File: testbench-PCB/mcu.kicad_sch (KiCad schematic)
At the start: 16 parts, among them J2 AVR-ISP-6, SW1 RESET, U1 ATmega2561-16A, Y1 X322516MLB4SI

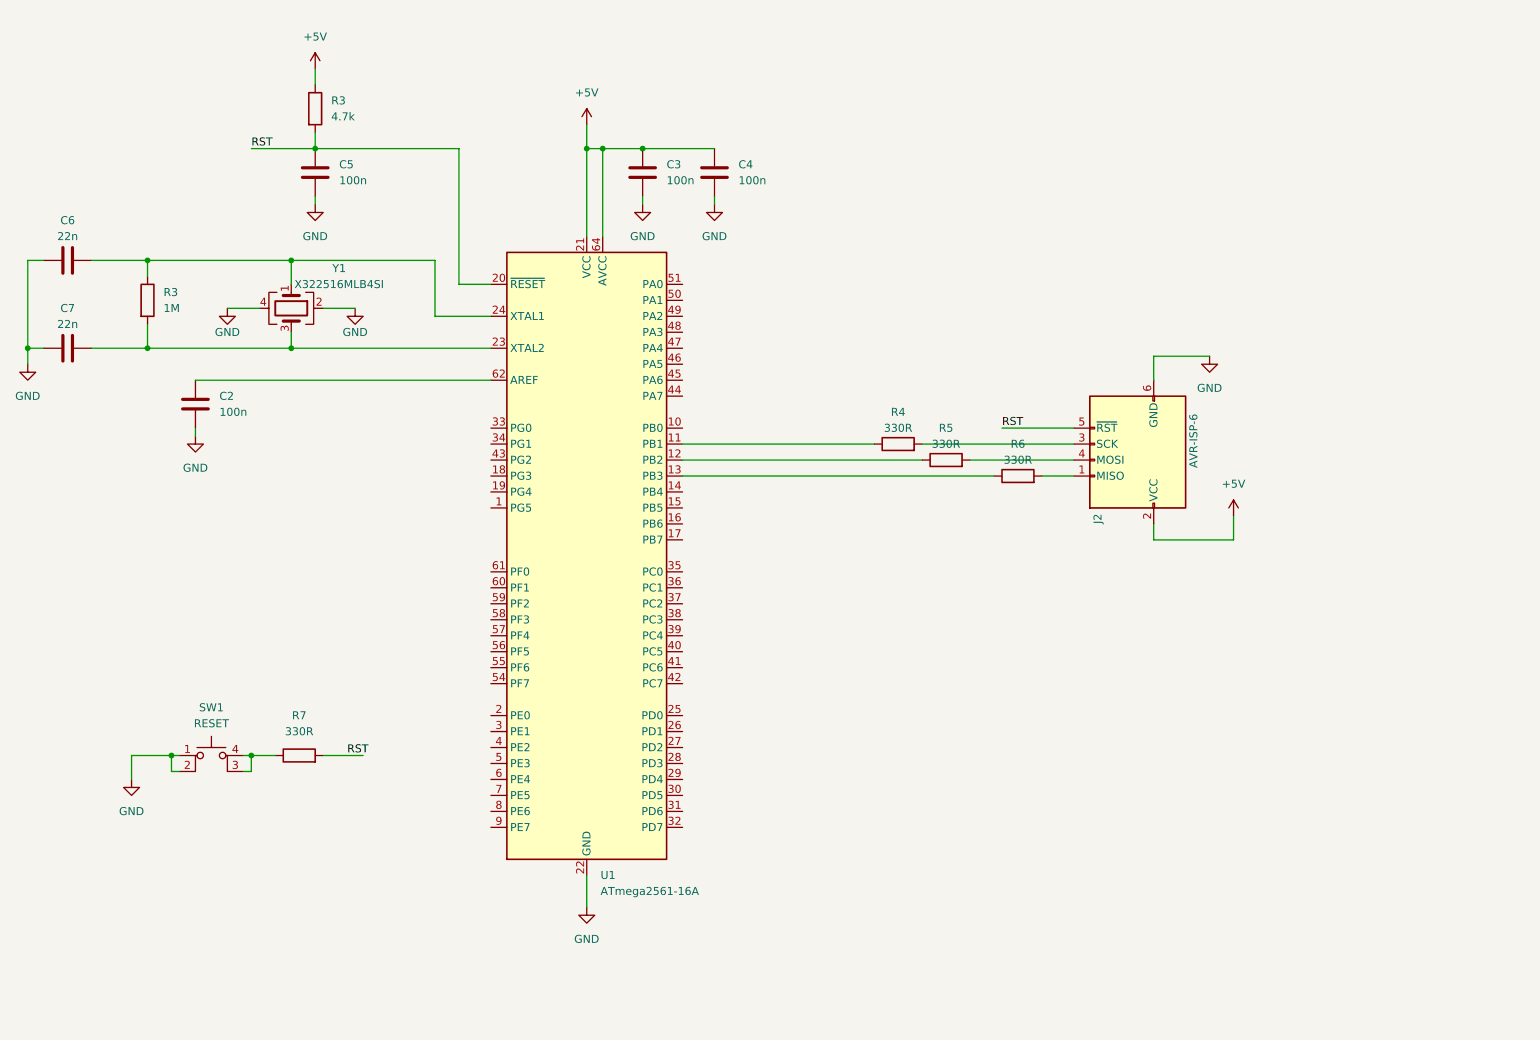
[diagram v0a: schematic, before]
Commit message: Added USB interface.
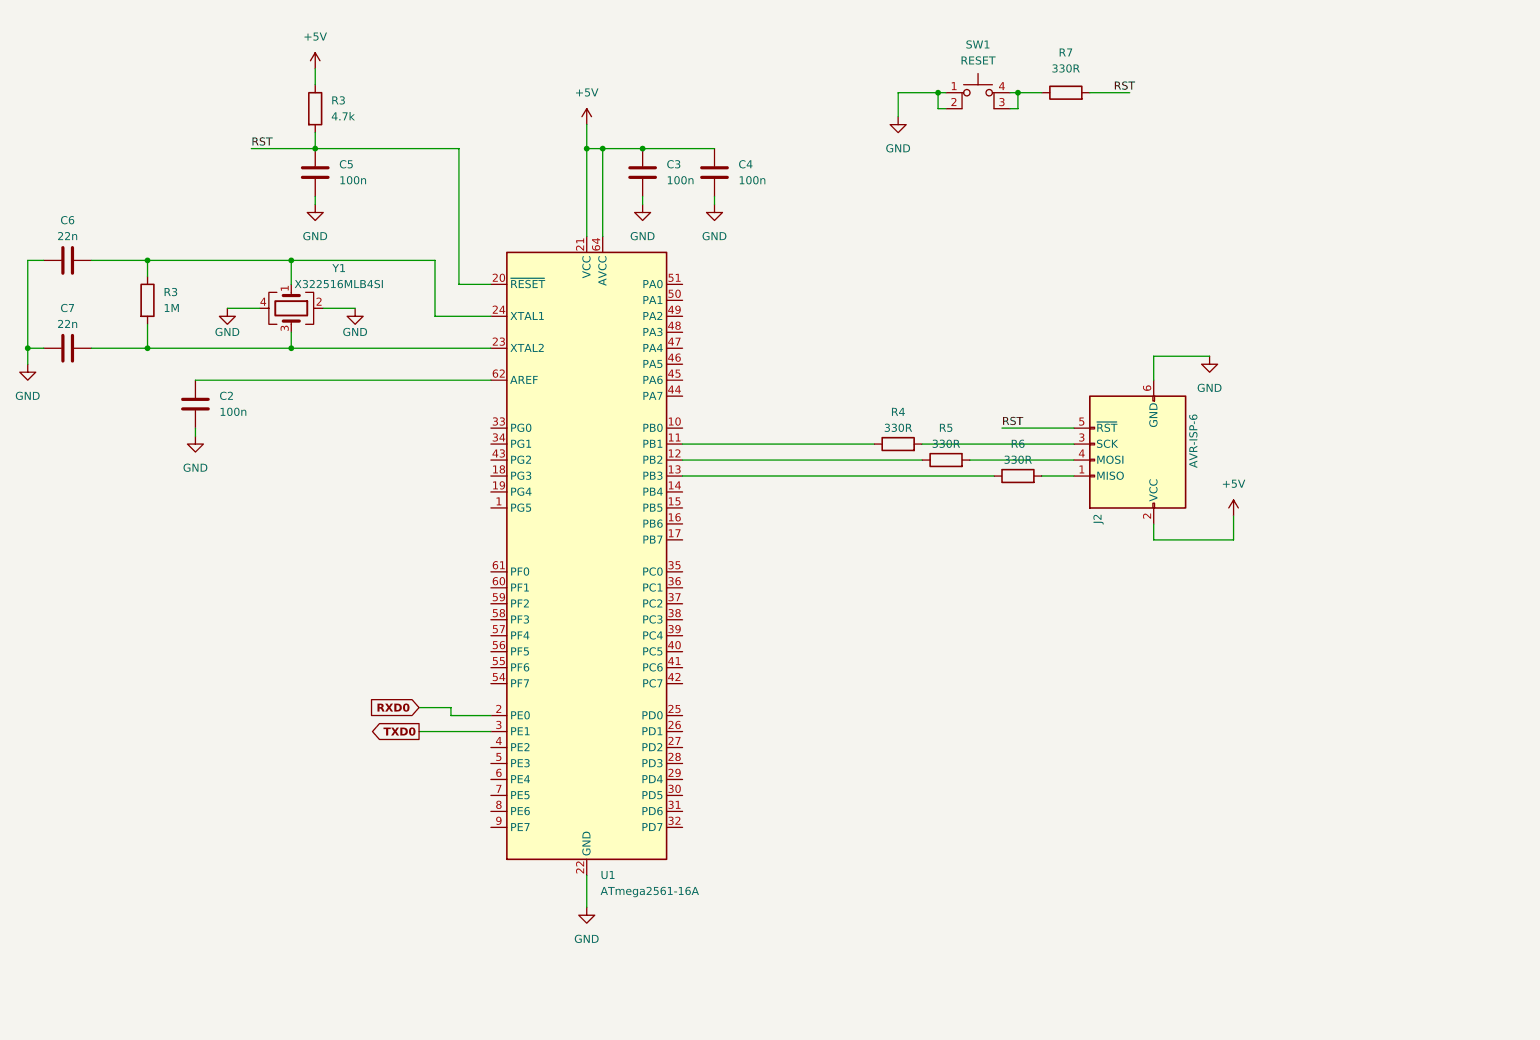
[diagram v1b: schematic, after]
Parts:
- R3, R4, R5, R6, R7: footprint (none) -> Resistor_SMD:R_0805_2012Metric
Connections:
- net RXD0: now reaches U1.2 (PE0)
- net TXD0: now reaches U1.3 (PE1)
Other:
- moved on the sheet: R7, SW1

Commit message: Added connection between some modules.
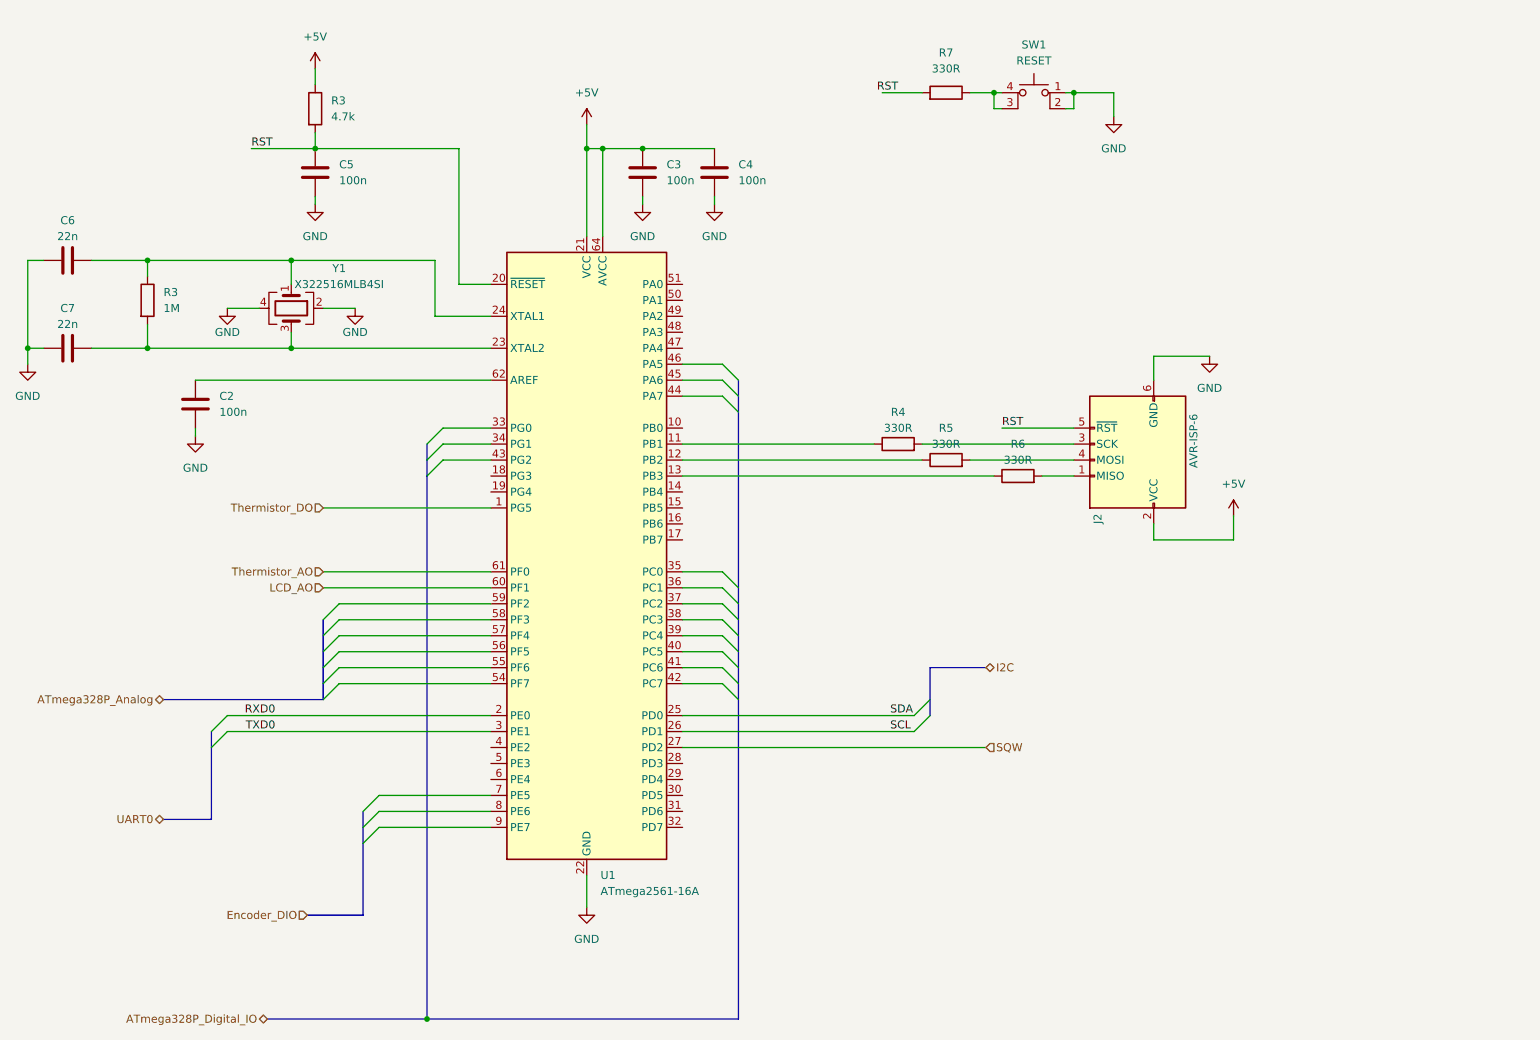
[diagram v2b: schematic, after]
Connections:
- net Thermistor_DO: now reaches U1.1 (PG5)
- net SDA: now reaches U1.25 (PD0)
- net SCL: now reaches U1.26 (PD1)
- net SQW: now reaches U1.27 (PD2)
- net LCD_AO: now reaches U1.60 (PF1)
- net Thermistor_AO: now reaches U1.61 (PF0)
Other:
- moved on the sheet: R7, SW1

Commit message: Finished connection between modules and MCU.
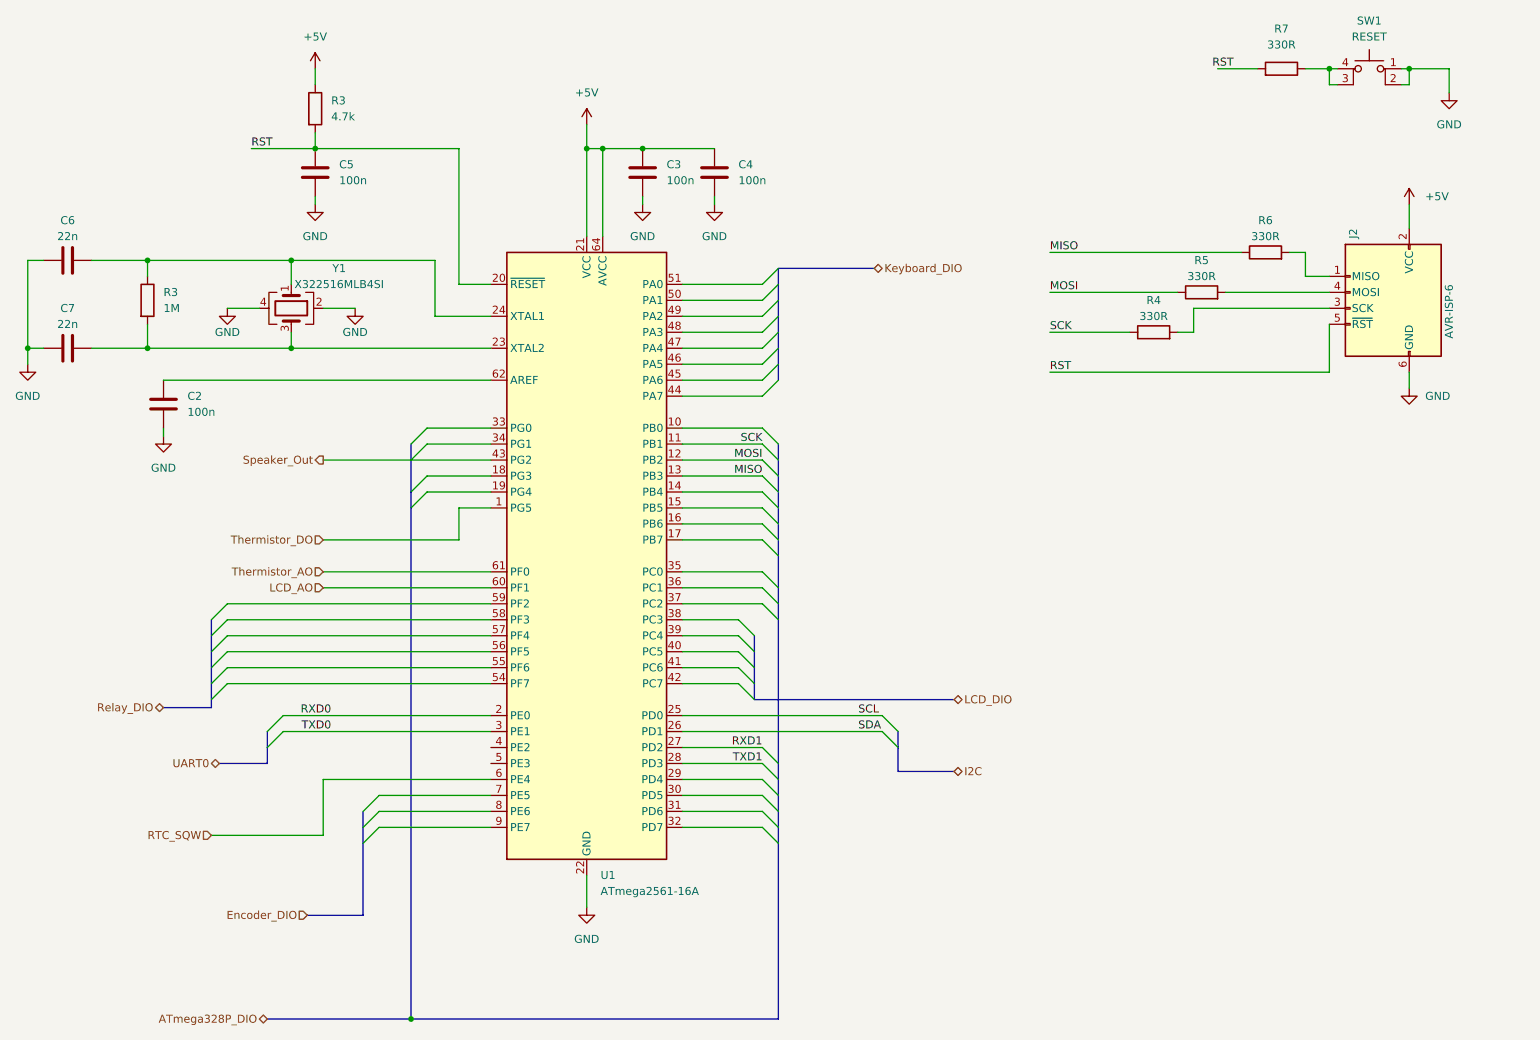
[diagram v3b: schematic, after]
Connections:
- net SCL: now also U1.25 (PD0); no longer U1.26 (PD1)
- net SDA: now also U1.26 (PD1); no longer U1.25 (PD0)
- net MOSI: now reaches R5.1, U1.12 (PB2)
- net SCK: now reaches R4.1, U1.11 (PB1)
- net MISO: now reaches R6.1, U1.13 (PB3)
- net TXD1: now reaches U1.28 (PD3)
- net Speaker_Out: now reaches U1.43 (PG2)
- net RTC_SQW: now reaches U1.6 (PE4)
- net SQW renamed RXD1
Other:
- moved on the sheet: C2, J2, R4, R5, R6, R7, SW1

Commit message: Added footprints to few parts.
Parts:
- C2, C3, C4, C5, C6, C7: footprint (none) -> Capacitor_SMD:C_0805_2012Metric
- J2: footprint (none) -> Connector_PinHeader_2.54mm:PinHeader_2x03_P2.54mm_Vertical
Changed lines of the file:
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@@
       (effects (font (size 1.27 1.27)) (justify left))
     )
-    (property "Footprint" "" (at 149.5552 53.34 0)
+    (property "Footprint" "Capacitor_SMD:C_0805_2012Metric" (at 149.5552 53.34 0)
       (effects (font (size 1.27 1.27)) hide)
     )
@@
       (effects (font (size 1.27 1.27)))
     )
-    (property "Footprint" "" (at 49.53 76.5048 0)
+    (property "Footprint" "Capacitor_SMD:C_0805_2012Metric" (at 49.53 76.5048 0)
       (effects (font (size 1.27 1.27)) hide)
     )
@@
       (effects (font (size 1.27 1.27)) (justify left))
     )
-    (property "Footprint" "" (at 138.1252 53.34 0)
+    (property "Footprint" "Capacitor_SMD:C_0805_2012Metric" (at 138.1252 53.34 0)
       (effects (font (size 1.27 1.27)) hide)
     )
@@
       (effects (font (size 1.27 1.27)))
     )
-    (property "Footprint" "" (at 49.53 62.5348 0)
+    (property "Footprint" "Capacitor_SMD:C_0805_2012Metric" (at 49.53 62.5348 0)
       (effects (font (size 1.27 1.27)) hide)
     )
@@
       (effects (font (size 1.27 1.27)) (justify left))
     )
-    (property "Footprint" "" (at 86.0552 53.34 0)
+    (property "Footprint" "Capacitor_SMD:C_0805_2012Metric" (at 86.0552 53.34 0)
       (effects (font (size 1.27 1.27)) hide)
     )
@@
       (effects (font (size 1.27 1.27)) (justify left))
     )
-    (property "Footprint" "" (at 61.9252 90.17 0)
+    (property "Footprint" "Capacitor_SMD:C_0805_2012Metric" (at 61.9252 90.17 0)
       (effects (font (size 1.27 1.27)) hide)
     )
@@
       (effects (font (size 1.27 1.27)) (justify right))
     )
-    (property "Footprint" "" (at 262.89 69.85 90)
-      (effects (font (size 1.27 1.27)) hide)
-    )
+    (property "Footprint" "Connector_PinHeader_2.54mm:PinHeader_2x03_P2.54mm_Vertical" (at 262.89 69.85 90)
+      (effects (font (size 1.27 1.27)) hide)
+    )

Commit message: Changed naming convention.
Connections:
- net RXD0 renamed UART0_RXD
- net SCL renamed I2C_SCL
- net SDA renamed I2C_SDA
- net TXD0 renamed UART0_TXD
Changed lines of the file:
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@@
     (stroke (width 0) (type default))
   )
-  (label "SDA" (at 171.45 138.43 0) (fields_autoplaced)
+  (label "I2C_SDA" (at 167.64 138.43 0) (fields_autoplaced)
     (effects (font (size 1.27 1.27)) (justify left bottom))
   )
@@
     (effects (font (size 1.27 1.27)) (justify right bottom))
   )
-  (label "SCL" (at 171.45 135.89 0) (fields_autoplaced)
+  (label "I2C_SCL" (at 167.64 135.89 0) (fields_autoplaced)
     (effects (font (size 1.27 1.27)) (justify left bottom))
   )
@@
     (effects (font (size 1.27 1.27)) (justify right bottom))
   )
-  (label "TXD0" (at 87.63 138.43 180) (fields_autoplaced)
+  (label "UART0_TXD" (at 90.17 138.43 180) (fields_autoplaced)
     (effects (font (size 1.27 1.27)) (justify right bottom))
   )
-  (label "RXD0" (at 87.63 135.89 180) (fields_autoplaced)
+  (label "UART0_RXD" (at 90.17 135.89 180) (fields_autoplaced)
     (effects (font (size 1.27 1.27)) (justify right bottom))
   )
@@
     (effects (font (size 1.27 1.27)) (justify left bottom))
   )
-  (hierarchical_label "LCD_DIO" (shape bidirectional) (at 186.69 133.35 0) (fields_autoplaced)
+  (hierarchical_label "LCD_D[0..6]" (shape bidirectional) (at 186.69 133.35 0) (fields_autoplaced)
     (effects (font (size 1.27 1.27)) (justify left))
   )
-  (hierarchical_label "I2C" (shape bidirectional) (at 186.69 144.78 0) (fields_autoplaced)
+  (hierarchical_label "{I2C}" (shape bidirectional) (at 186.69 144.78 0) (fields_autoplaced)
     (effects (font (size 1.27 1.27)) (justify left))
   )
-  (hierarchical_label "Relay_DIO" (shape bidirectional) (at 60.96 134.62 180) (fields_autoplaced)
+  (hierarchical_label "{RELAY_IO}" (shape bidirectional) (at 60.96 134.62 180) (fields_autoplaced)
     (effects (font (size 1.27 1.27)) (justify right))
   )
@@
     (effects (font (size 1.27 1.27)) (justify right))
   )
-  (hierarchical_label "Encoder_DIO" (shape input) (at 83.82 167.64 180) (fields_autoplaced)
+  (hierarchical_label "{Encoder_DIO}" (shape input) (at 83.82 167.64 180) (fields_autoplaced)
     (effects (font (size 1.27 1.27)) (justify right))
   )
-  (hierarchical_label "UART0" (shape bidirectional) (at 69.85 143.51 180) (fields_autoplaced)
+  (hierarchical_label "{UART0}" (shape bidirectional) (at 69.85 143.51 180) (fields_autoplaced)
     (effects (font (size 1.27 1.27)) (justify right))
   )
@@
     (effects (font (size 1.27 1.27)) (justify right))
   )
-  (hierarchical_label "ATmega328P_DIO" (shape bidirectional) (at 77.47 184.15 180) (fields_autoplaced)
+  (hierarchical_label "DUT[0..20]" (shape bidirectional) (at 77.47 184.15 180) (fields_autoplaced)
     (effects (font (size 1.27 1.27)) (justify right))
   )
-  (hierarchical_label "Keyboard_DIO" (shape bidirectional) (at 173.99 64.77 0) (fields_autoplaced)
+  (hierarchical_label "KEY_D[0..7]" (shape bidirectional) (at 173.99 64.77 0) (fields_autoplaced)
     (effects (font (size 1.27 1.27)) (justify left))
   )
